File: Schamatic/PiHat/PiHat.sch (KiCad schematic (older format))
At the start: 44 parts, among them J1 +45V, J10 GND, J11 GND, J12 SW1, J13 SW2, J14 MOUNT, J15 MOUNT, J16 MOUNT, J17 MOUNT, J2 +45V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

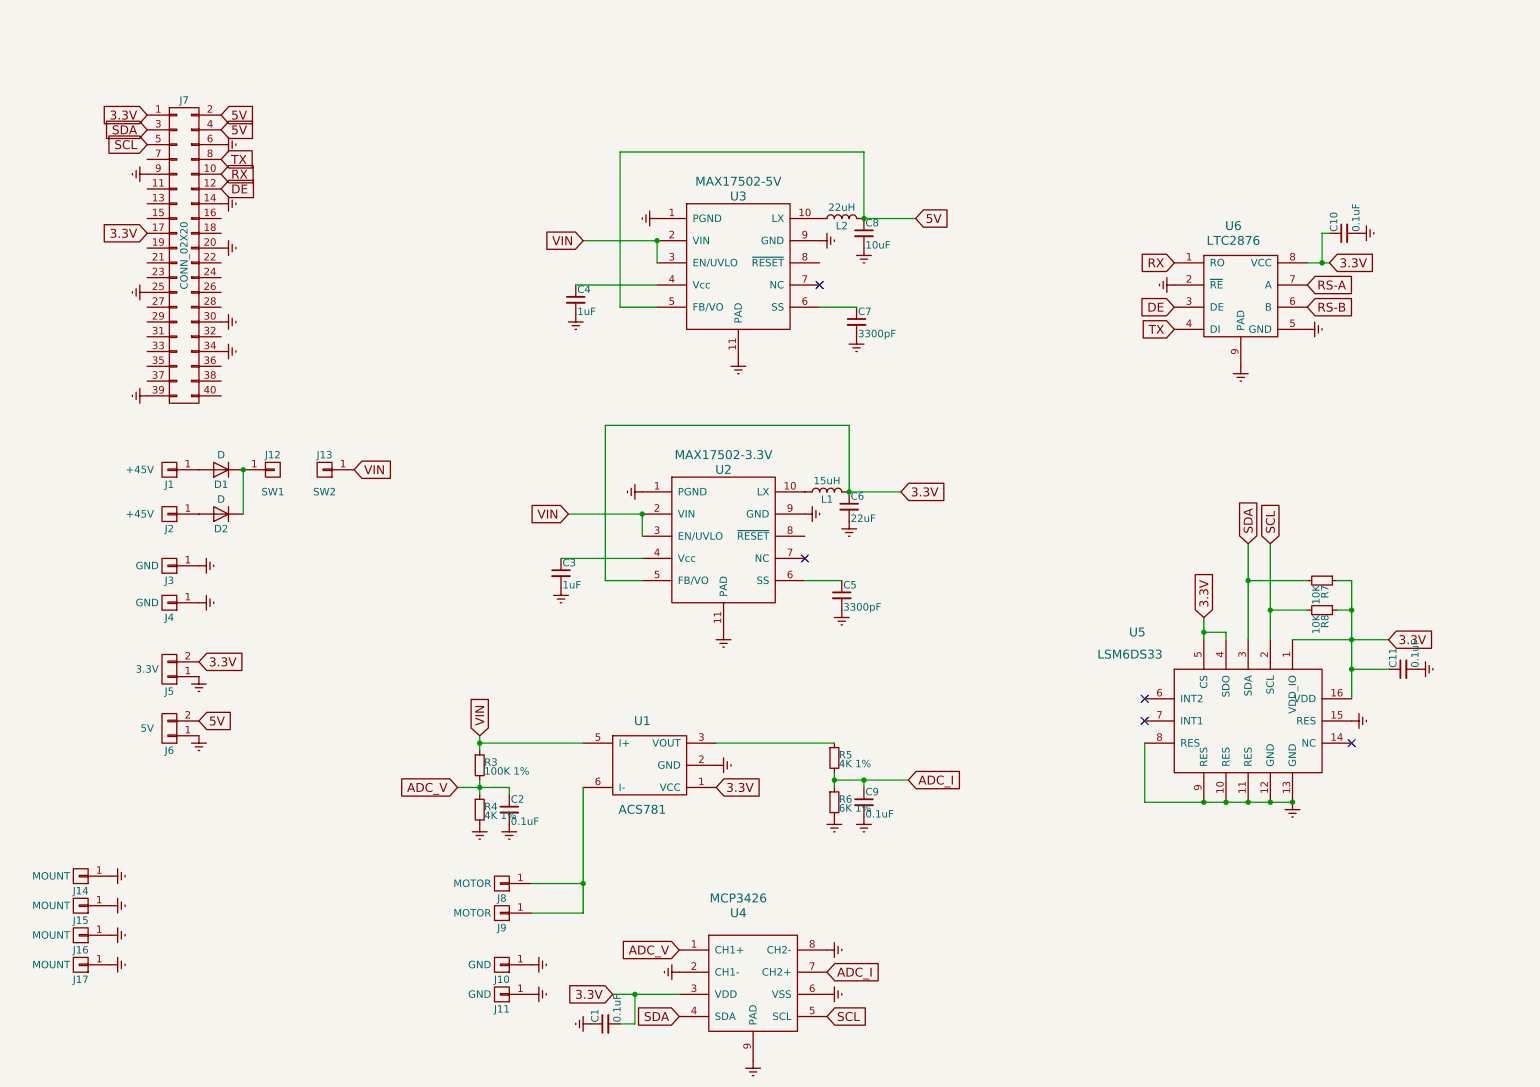
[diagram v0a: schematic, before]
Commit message: starting AS548 sensor
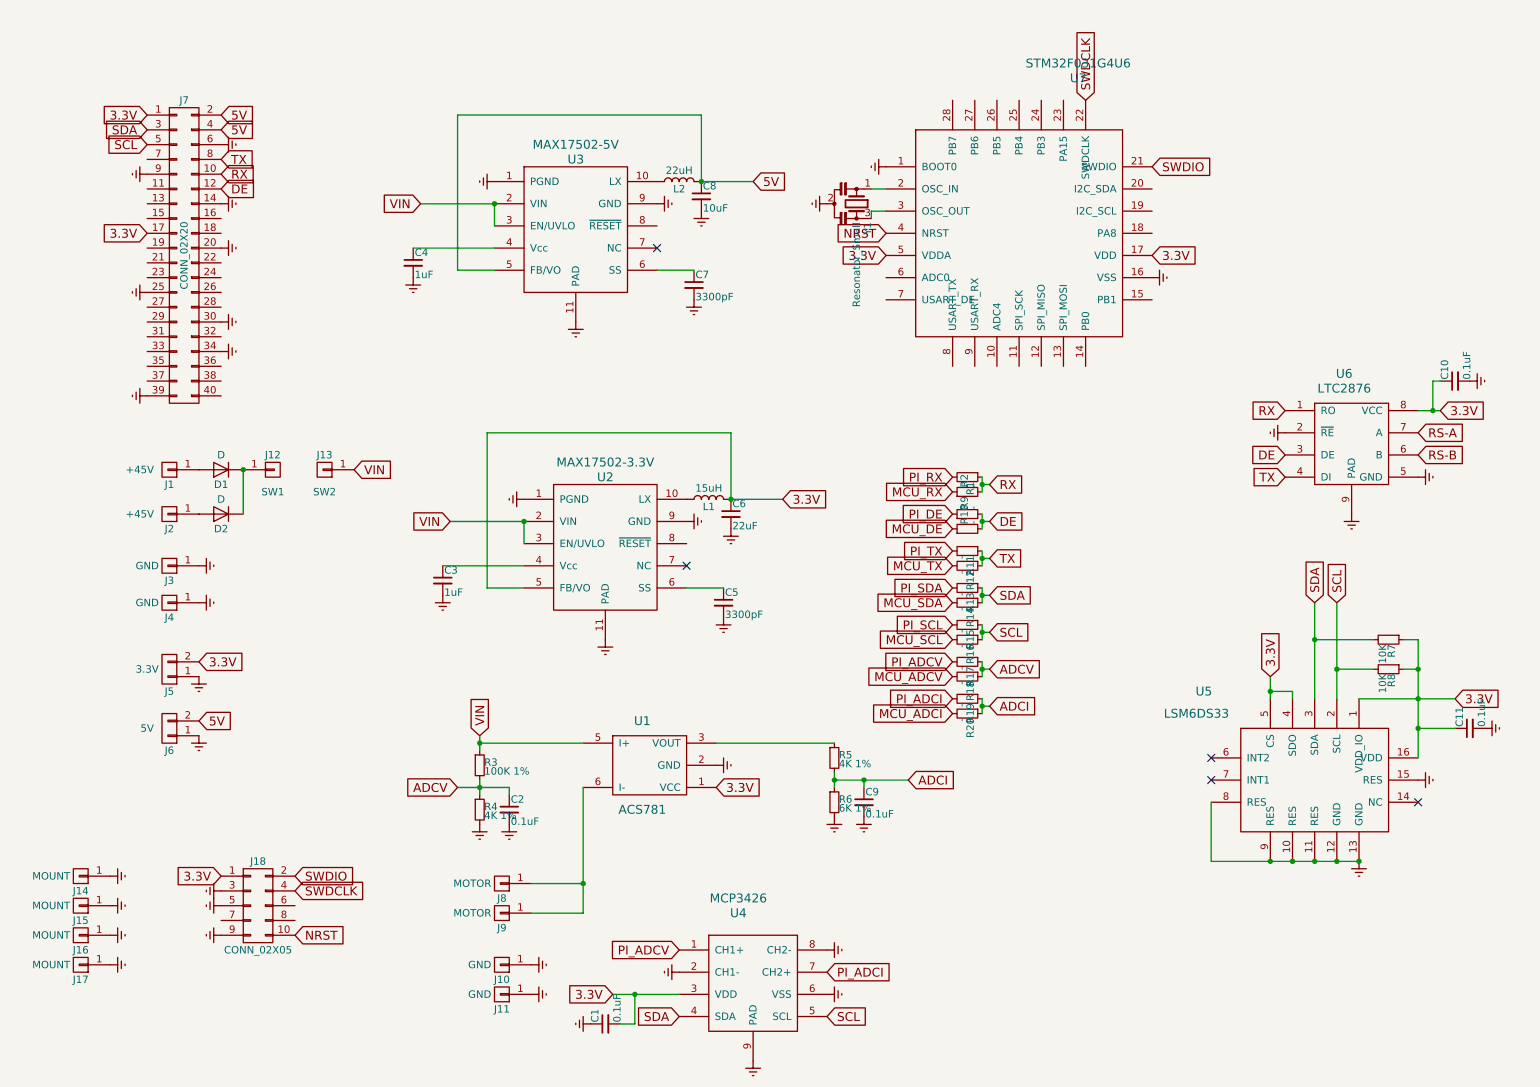
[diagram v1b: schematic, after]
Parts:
- added J18: CONN_02X05, Pin_Headers:Pin_Header_Straight_2x05_Pitch1.27mm, symbol CONN_02X05
- added R1, R10, R11, R12, R13, R14, R15, R16, R17, R18, R19, R2, R20, R9: -, Dizzy:SOLDER-SWITCH, symbol R_Small
- added U7: STM32F031G4U6, symbol STM32F031G4U6
- added Y1: Resonator_Small, Dizzy:OSC_CSTCE16M0V53-R0, symbol Resonator_Small
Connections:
- net 3.3V: now also J18.1 (P1), U7.17 (VDD), U7.5 (VDDA)
- net DE: now also R10.2, R9.2
- net Earth: now also J18.3 (P3), J18.5 (P5), J18.9 (P9), U7.1 (BOOT0), U7.16 (VSS), Y1.2
- net RX: now also R1.1, R2.2
- net SCL: now also R15.1, R16.1
- net SDA: now also R13.1, R14.1
- net TX: now also R11.1, R12.1
- net ADC_I renamed ADCI
- net ADCI: now also R19.1, R20.1; no longer U4.7 (CH2+)
- net ADC_V renamed ADCV
- net ADCV: now also R17.1, R18.1; no longer U4.1 (CH1+)
- new net: U7.2 (OSC_IN), Y1.1
- new net: U7.3 (OSC_OUT), Y1.3
- new net MCU_ADCI: R20.2
- new net MCU_ADCV: R18.2
- new net MCU_DE: R10.1
- new net MCU_RX: R2.1
- new net MCU_SCL: R16.2
- new net MCU_SDA: R14.2
- new net MCU_TX: R12.2
- new net NRST: J18.10 (P10), U7.4 (NRST)
- new net PI_ADCI: R19.2, U4.7 (CH2+)
- new net PI_ADCV: R17.2, U4.1 (CH1+)
- new net PI_DE: R9.1
- new net PI_RX: R1.2
- new net PI_SCL: R15.2
- new net PI_SDA: R13.2
- new net PI_TX: R11.2
- new net SWDCLK: J18.4 (P4), U7.22 (SWDCLK)
- new net SWDIO: J18.2 (P2), U7.21 (SWDIO)
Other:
- moved on the sheet: C10, C11, C3, C4, C5, C6, C7, C8, L1, L2, R7, R8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

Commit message: Pi hat more or less ready
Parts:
- removed R1, R10, R11, R12, R13, R14, R15, R16, R17, R18, R19, R2, R20, R9: -, Dizzy:SOLDER-SWITCH, symbol R_Small
- added C12: 0.1uF, Capacitors_SMD:C_0603, symbol C_Small
- added J19: ADCV, Dizzy:SOLDER-SWITCH, symbol CONN_01X03
- added J20: ADCI, Dizzy:SOLDER-SWITCH, symbol CONN_01X03
- added J21: RX, Dizzy:SOLDER-SWITCH, symbol CONN_01X03
- added J22: DE, Dizzy:SOLDER-SWITCH, symbol CONN_01X03
- added J23: TX, Dizzy:SOLDER-SWITCH, symbol CONN_01X03
- added J24: SDA, Dizzy:SOLDER-SWITCH, symbol CONN_01X03
- added J25: SCL, Dizzy:SOLDER-SWITCH, symbol CONN_01X03
- added J26, J27: CONN_01X02, Pin_Headers:Pin_Header_Straight_2x01_Pitch2.54mm, symbol CONN_01X02
- U7: footprint (none) -> Dizzy:STM32F031G4U6
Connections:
- net 3.3V: now also C12.1
- net ADCI: now also J20.2 (P2)
- net ADCV: now also J19.2 (P2)
- net DE: now also J22.2 (P2); no longer J7.12 (P12)
- net Earth: now also C12.2
- net MCU_ADCI: now also U7.6 (ADC0), J20.3 (P3)
- net MCU_ADCV: now also U7.10 (ADC4), J19.3 (P3)
- net MCU_DE: now also U7.7 (USART_DE), J22.3 (P3)
- net MCU_RX: now also U7.9 (USART_RX), J21.3 (P3)
- net MCU_SCL: now also U7.19 (I2C_SCL), J25.3 (P3)
- net MCU_SDA: now also U7.20 (I2C_SDA), J24.3 (P3)
- net MCU_TX: now also U7.8 (USART_TX), J23.3 (P3)
- net PI_ADCI: now also J20.1 (P1)
- net PI_ADCV: now also J19.1 (P1)
- net PI_DE: now also J7.12 (P12), J22.1 (P1)
- net PI_RX: now also J7.10 (P10), J21.1 (P1)
- net PI_SCL: now also J7.5 (P5), J25.1 (P1)
- net PI_SDA: now also J7.3 (P3), J24.1 (P1)
- net PI_TX: now also J7.8 (P8), J23.1 (P1)
- net RS-A: now also J26.2 (P2), J27.2 (P2)
- net RS-B: now also J26.1 (P1), J27.1 (P1)
- net RX: now also J21.2 (P2); no longer J7.10 (P10)
- net SCL: now also J25.2 (P2); no longer J7.5 (P5)
- net SDA: now also J24.2 (P2); no longer J7.3 (P3)
- net TX: now also J23.2 (P2); no longer J7.8 (P8)
- net MOSI: now reaches J7.19 (P19)
- net MOSI: now also U7.13 (SPI_MOSI)
- net MISO: now reaches J7.21 (P21)
- net MISO: now also U7.12 (SPI_MISO)
- net SCK: now reaches J7.23 (P23)
- net SCK: now also U7.11 (SPI_SCK)
- net WRDY: now reaches J7.29 (P29)
- net WRDY: now also U7.27 (PB6)
- net RRDY: now reaches J7.31 (P31)
- net RRDY: now also U7.26 (PB5)
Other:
- moved on the sheet: J3, J4, J5, J6

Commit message: fixes to the boards
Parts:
- added C13: 10uF, Capacitors_SMD:C_1206, symbol C_Small
- added D3: 47V, Diodes_SMD:D_SOD-123F, symbol D_Zener_Small
- C6, C8: footprint Capacitors_SMD:C_0805 -> Capacitors_SMD:C_1206
- D2: footprint Diodes_SMD:D_SMA -> Diodes_SMD:D_SOD-323F
- L1, L2: footprint Inductors_SMD:L_1812 -> Dizzy:Inductor-1812
- Y1: footprint Dizzy:OSC_CSTCE16M0V53-R0 -> Dizzy:Oscillator
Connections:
- net Earth: now also C13.1, D3.2 (A)
- net VIN: now also D2.1 (K), C13.2, D3.1 (K); no longer J13.1 (P1), R3.1, U1.5 (I+)
- net GPIO13: now reaches J7.33 (P33)
- net GPIO13: now also U7.25 (PB4)
- net GPIO19: now reaches J7.35 (P35)
- net GPIO19: now also U7.24 (PB3)
- net GPIO26: now reaches J7.37 (P37)
- net GPIO26: now also U7.23 (PA15)
- net at J2.1 (P1): now also D1.1 (K), J12.1 (P1); no longer D2.2 (A)
- new net: D2.2 (A), J13.1 (P1), R3.1, U1.5 (I+)
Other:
- moved on the sheet: D1, J1, J12, J13, J2, J3, J4, J5, J6

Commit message: starting PiHat firmware
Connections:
- net MCU_ADCV: now also U7.14 (PB0); no longer U7.10 (ADC4)
- net MCU_CS: now reaches J7.24 (P24)
- net MCU_CS: now also U7.10 (ADC4)
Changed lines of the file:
@@
 Text GLabel 6600 2250 0    60   Input ~ 0
 MCU_ADCI
-Text GLabel 7350 2850 3    60   Input ~ 0
+Text GLabel 7950 2850 3    60   Input ~ 0
 MCU_ADCV
 Text GLabel 7050 2850 3    60   Input ~ 0
@@
 Text GLabel 7800 1050 1    60   Input ~ 0
 GPIO26
+Text GLabel 7350 2850 3    60   Input ~ 0
+MCU_CS
+Text GLabel 2100 2250 2    60   Input ~ 0
+MCU_CS
 $EndSCHEMATC

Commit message: saving
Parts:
- removed C1: 0.1uF, Capacitors_SMD:C_0603, symbol C_Small
- removed J19: ADCV, Dizzy:SOLDER-SWITCH, symbol CONN_01X03
- removed J20: ADCI, Dizzy:SOLDER-SWITCH, symbol CONN_01X03
- removed J21: RX, Dizzy:SOLDER-SWITCH, symbol CONN_01X03
- removed J22: DE, Dizzy:SOLDER-SWITCH, symbol CONN_01X03
- removed J23: TX, Dizzy:SOLDER-SWITCH, symbol CONN_01X03
- removed J24: SDA, Dizzy:SOLDER-SWITCH, symbol CONN_01X03
- removed J25: SCL, Dizzy:SOLDER-SWITCH, symbol CONN_01X03
- removed L1: 15uH, Dizzy:Inductor-1812, symbol L
- removed L2: 22uH, Dizzy:Inductor-1812, symbol L
- removed U2: MAX17502-3.3V, Housings_DFN_QFN:DFN-10-1EP_2x3mm_Pitch0.5mm, symbol MAX17502
- removed U3: MAX17502-5V, Housings_DFN_QFN:DFN-10-1EP_2x3mm_Pitch0.5mm, symbol MAX17502
- removed U4: MCP3426, Dizzy:8-DFN-2x3, symbol MCP3426
- added D4, D5: D_Small, Diodes_SMD:D_SOD-323, symbol D_Small
- added D6, D7: LED_Small, LEDs:LED_0603, symbol LED_Small
- added J19: SDA, Dizzy:1pin, symbol CONN_01X01
- added J20: SCL, Dizzy:1pin, symbol CONN_01X01
- added J21: ADCI, Dizzy:1pin, symbol CONN_01X01
- added J22: ADCV, Dizzy:1pin, symbol CONN_01X01
- added J23: DE, Dizzy:1pin, symbol CONN_01X01
- added J24: TX, Dizzy:1pin, symbol CONN_01X01
- added J25: RX, Dizzy:1pin, symbol CONN_01X01
- added L1, L2: 47uH, Dizzy:Inductor-1812, symbol L_Small
- added R1, R2: 22k, Resistors_SMD:R_0603, symbol R_Small
- added R10, R9: 370, Resistors_SMD:R_0603, symbol R_Small
- added U2: IFX91041 - 5V, Housings_SOIC:HTSOP-8-1EP_3.9x4.9mm_Pitch1.27mm_ThermalVias, symbol IFX91041
- added U3: IFX91041 - 3.3V, Housings_SOIC:HTSOP-8-1EP_3.9x4.9mm_Pitch1.27mm_ThermalVias, symbol IFX91041
- C13: value 10uF -> 1uF
- C3, C4: value 1uF -> 22nF
- C5: value 3300pF -> 220nF
- C6: value 22uF -> 220nF; footprint Capacitors_SMD:C_1206 -> Capacitors_SMD:C_0603
- C7: value 3300pF -> 100uF; footprint Capacitors_SMD:C_0603 -> Capacitors_SMD:C_1206
- C8: value 10uF -> 100uF
- J14, J15, J16, J17: footprint Connectors:1pin -> Dizzy:1pin
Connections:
- net MCU_ADCI is gone; now on net ADCI: U7.6 (ADC0)
- net MCU_ADCV is gone; now on net ADCV: U7.14 (PB0)
- net MCU_DE is gone; now on net DE: U7.7 (USART_DE)
- net MCU_RX is gone; now on net RX: U7.9 (USART_RX)
- net MCU_SCL is gone; now on net SCL: U7.19 (I2C_SCL)
- net MCU_SDA is gone; now on net SDA: U7.20 (I2C_SDA)
- net MCU_TX is gone; now on net TX: U7.8 (USART_TX)
- net 3.3V: now also C8.1, L2.2, U3.4 (FB); no longer C6.1
- net 5V: now also C7.1, L1.2, U2.4 (FB); no longer C8.1, J7.2 (P2), J7.4 (P4)
- net ADCI: now also J21.1 (P1)
- net ADCV: now also J22.1 (P1)
- net DE: now also J23.1 (P1)
- net Earth: now also D4.2 (A), D5.2 (A), R10.1, R9.1, U2.1 (SYNC), U2.2 (GND), U2.9 (GND), U3.1 (SYNC), U3.2 (GND), U3.9 (GND); no longer C5.2, C6.2
- net RX: now also J25.1 (P1)
- net SCL: now also J20.1 (P1)
- net SDA: now also J19.1 (P1)
- net TX: now also J24.1 (P1)
- net VIN: now also U2.7 (EN), U2.8 (VS), U3.7 (EN), U3.8 (VS)
- net at C4.1: now also R2.2
- net at C3.1: now also R1.2
- net at C5.1: now also U2.5 (BDS)
- net MCU_CS renamed CS
- net PI_DE: no longer names the net of J7.12 (P12)
- net PI_RX: no longer names the net of J7.10 (P10)
- net PI_SCL: no longer names the net of J7.5 (P5)
- net PI_SDA: no longer names the net of J7.3 (P3)
- net PI_TX: no longer names the net of J7.8 (P8)
- net RRDY renamed RECVRDY
- net RECVRDY: now also D7.2 (A)
- net WRDY renamed RESPRDY
- net RESPRDY: now also D6.2 (A)
- new net: R1.1, U2.3 (COMP)
- new net: C5.2, D4.1 (K), L1.1, U2.6 (BUO)
- new net: R2.1, U3.3 (COMP)
- new net: C6.1, U3.5 (BDS)
- new net: C6.2, D5.1 (K), L2.1, U3.6 (BUO)
- new net: D6.1 (K), R9.2
- new net: D7.1 (K), R10.2
- no-connect marks 5 -> 3
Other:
- moved on the sheet: J18
